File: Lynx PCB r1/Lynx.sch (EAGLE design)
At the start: 109 parts, among them IC1 LM321MF, IC3 ICL7660, Q1 8MHz

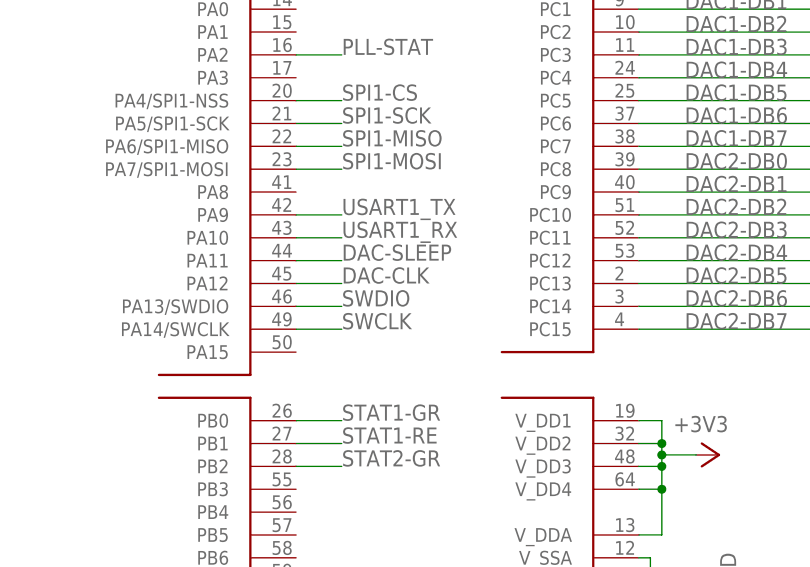
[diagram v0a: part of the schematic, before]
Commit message: Finished first pass of silk
Finished organizing the first revision of the artwork. Added pin names
to all busses. Created a dac-clk test pin
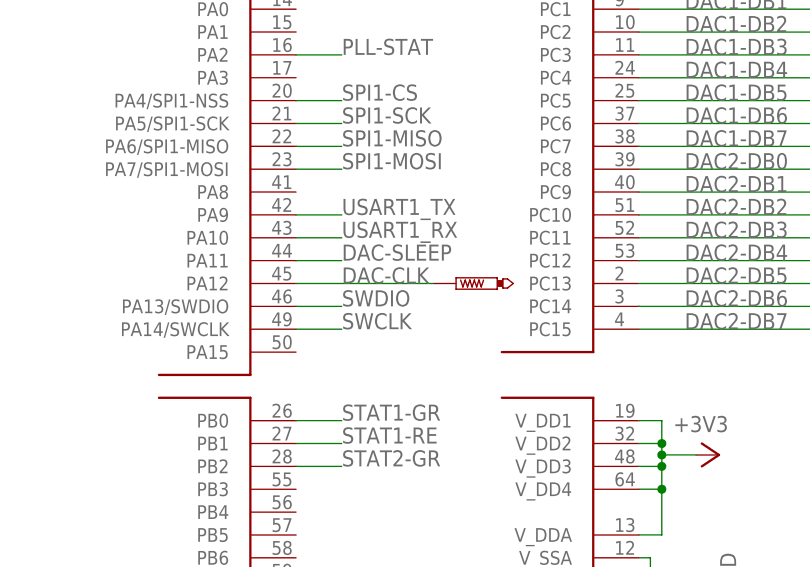
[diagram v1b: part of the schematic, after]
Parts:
- added DAC-CLK: PTR1PAD1-13Y, testpad:PTR1PAD1-13Y
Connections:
- net DAC-CLK: now also DAC-CLK.TP
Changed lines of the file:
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@@
 <grid distance="0.05" unitdist="inch" unit="inch" style="lines" multiple="1" display="no" altdistance="0.01" altunitdist="inch" altunit="inch"/>
 <layers>
-<layer number="1" name="Top" color="4" fill="1" visible="no" active="no"/>
-<layer number="2" name="Route2" color="1" fill="3" visible="no" active="no"/>
-<layer number="3" name="Route3" color="4" fill="3" visible="no" active="no"/>
-<layer number="4" name="Route4" color="1" fill="4" visible="no" active="no"/>
-<layer number="5" name="Route5" color="4" fill="4" visible="no" active="no"/>
-<layer number="6" name="Route6" color="1" fill="8" visible="no" active="no"/>
-<layer number="7" name="Route7" color="4" fill="8" visible="no" active="no"/>
-<layer number="8" name="Route8" color="1" fill="2" visible="no" active="no"/>
-<layer number="9" name="Route9" color="4" fill="2" visible="no" active="no"/>
-<layer number="10" name="Route10" color="1" fill="7" visible="no" active="no"/>
-<layer number="11" name="Route11" color="4" fill="7" visible="no" active="no"/>
-<layer number="12" name="Route12" color="1" fill="5" visible="no" active="no"/>
-<layer number="13" name="Route13" color="4" fill="5" visible="no" active="no"/>
-<layer number="14" name="Route14" color="1" fill="6" visible="no" active="no"/>
-<layer number="15" name="Route15" color="4" fill="6" visible="no" active="no"/>
-<layer number="16" name="Bottom" color="1" fill="1" visible="no" active="no"/>
-<layer number="17" name="Pads" color="2" fill="1" visible="no" active="no"/>
-<layer number="18" name="Vias" color="2" fill="1" visible="no" active="no"/>
-<layer number="19" name="Unrouted" color="6" fill="1" visible="no" active="no"/>
-<layer number="20" name="Dimension" color="15" fill="1" visible="no" active="no"/>
-<layer number="21" name="tPlace" color="7" fill="1" visible="no" active="no"/>
-<layer number="22" name="bPlace" color="7" fill="1" visible="no" active="no"/>
-<layer number="23" name="tOrigins" color="15" fill="1" visible="no" active="no"/>
-<layer number="24" name="bOrigins" color="15" fill="1" visible="no" active="no"/>
-<layer number="25" name="tNames" color="7" fill="1" visible="no" active="no"/>
-<layer number="26" name="bNames" color="7" fill="1" visible="no" active="no"/>
-<layer number="27" name="tValues" color="7" fill="1" visible="no" active="no"/>
-<layer number="28" name="bValues" color="7" fill="1" visible="no" active="no"/>
+<layer number="1" name="Top" color="4" fill="1" visible="yes" active="no"/>
+<layer number="2" name="Route2" color="1" fill="3" visible="yes" active="no"/>
+<layer number="3" name="Route3" color="4" fill="3" visible="yes" active="no"/>
+<layer number="4" name="Route4" color="1" fill="4" visible="yes" active="no"/>
+<layer number="5" name="Route5" color="4" fill="4" visible="yes" active="no"/>
+<layer number="6" name="Route6" color="1" fill="8" visible="yes" active="no"/>
+<layer number="7" name="Route7" color="4" fill="8" visible="yes" active="no"/>
+<layer number="8" name="Route8" color="1" fill="2" visible="yes" active="no"/>
+<layer number="9" name="Route9" color="4" fill="2" visible="yes" active="no"/>
+<layer number="10" name="Route10" color="1" fill="7" visible="yes" active="no"/>
+<layer number="11" name="Route11" color="4" fill="7" visible="yes" active="no"/>
+<layer number="12" name="Route12" color="1" fill="5" visible="yes" active="no"/>
+<layer number="13" name="Route13" color="4" fill="5" visible="yes" active="no"/>
+<layer number="14" name="Route14" color="1" fill="6" visible="yes" active="no"/>
+<layer number="15" name="Route15" color="4" fill="6" visible="yes" active="no"/>
+<layer number="16" name="Bottom" color="1" fill="1" visible="yes" active="no"/>
+<layer number="17" name="Pads" color="2" fill="1" visible="yes" active="no"/>
+<layer number="18" name="Vias" color="2" fill="1" visible="yes" active="no"/>
+<layer number="19" name="Unrouted" color="6" fill="1" visible="yes" active="no"/>
+<layer number="20" name="Dimension" color="15" fill="1" visible="yes" active="no"/>
+<layer number="21" name="tPlace" color="7" fill="1" visible="yes" active="no"/>
+<layer number="22" name="bPlace" color="7" fill="1" visible="yes" active="no"/>
+<layer number="23" name="tOrigins" color="15" fill="1" visible="yes" active="no"/>
+<layer number="24" name="bOrigins" color="15" fill="1" visible="yes" active="no"/>
+<layer number="25" name="tNames" color="7" fill="1" visible="yes" active="no"/>
+<layer number="26" name="bNames" color="7" fill="1" visible="yes" active="no"/>
+<layer number="27" name="tValues" color="7" fill="1" visible="yes" active="no"/>
+<layer number="28" name="bValues" color="7" fill="1" visible="yes" active="no"/>
 <layer number="29" name="tStop" color="7" fill="3" visible="no" active="no"/>
 <layer number="30" name="bStop" color="7" fill="6" visible="no" active="no"/>
@@
 <layer number="35" name="tGlue" color="7" fill="4" visible="no" active="no"/>
 <layer number="36" name="bGlue" color="7" fill="5" visible="no" active="no"/>
-<layer number="37" name="tTest" color="7" fill="1" visible="no" active="no"/>
-<layer number="38" name="bTest" color="7" fill="1" visible="no" active="no"/>
+<layer number="37" name="tTest" color="7" fill="1" visible="yes" active="no"/>
+<layer number="38" name="bTest" color="7" fill="1" visible="yes" active="no"/>
 <layer number="39" name="tKeepout" color="4" fill="11" visible="no" active="no"/>
 <layer number="40" name="bKeepout" color="1" fill="11" visible="no" active="no"/>
@@
 <layer number="44" name="Drills" color="7" fill="1" visible="no" active="no"/>
 <layer number="45" name="Holes" color="7" fill="1" visible="no" active="no"/>
-<layer number="46" name="Milling" color="3" fill="1" visible="no" active="no"/>
-<layer number="47" name="Measures" color="7" fill="1" visible="no" active="no"/>
-<layer number="48" name="Document" color="7" fill="1" visible="no" active="no"/>
-<layer number="49" name="Reference" color="7" fill="1" visible="no" active="no"/>
-<layer number="50" name="dxf" color="7" fill="1" visible="no" active="no"/>
-<layer number="51" name="tDocu" color="7" fill="1" visible="no" active="no"/>
-<layer number="52" name="bDocu" color="7" fill="1" visible="no" active="no"/>
-<layer number="53" name="tGND_GNDA" color="7" fill="9" visible="no" active="no"/>
-<layer number="54" name="bGND_GNDA" color="1" fill="9" visible="no" active="no"/>
-<layer number="56" name="wert" color="7" fill="1" visible="no" active="no"/>
+<layer number="46" name="Milling" color="3" fill="1" visible="yes" active="no"/>
+<layer number="47" name="Measures" color="7" fill="1" visible="yes" active="no"/>
+<layer number="48" name="Document" color="7" fill="1" visible="yes" active="no"/>
+<layer number="49" name="Reference" color="7" fill="1" visible="yes" active="no"/>
+<layer number="50" name="dxf" color="7" fill="1" visible="yes" active="no"/>
+<layer number="51" name="tDocu" color="7" fill="1" visible="yes" active="no"/>
+<layer number="52" name="bDocu" color="7" fill="1" visible="yes" active="no"/>
+<layer number="53" name="tGND_GNDA" color="7" fill="9" visible="yes" active="no"/>
+<layer number="54" name="bGND_GNDA" color="1" fill="9" visible="yes" active="no"/>
+<layer number="56" name="wert" color="7" fill="1" visible="yes" active="no"/>
 <layer number="91" name="Nets" color="2" fill="1" visible="yes" active="yes"/>
 <layer number="92" name="Busses" color="1" fill="1" visible="yes" active="yes"/>
@@
 <part name="SUPPLY59" library="supply2" deviceset="GND" device=""/>
 <part name="JP11" library="pinhead" deviceset="PINHD-1X2" device="" value="Power In"/>
+<part name="DAC-CLK" library="testpad" deviceset="PTR1" device="PAD1-13Y" value="PTR1PAD1-13Y"/>
 </parts>
 <sheets>
@@
 <instance part="SUPPLY59" gate="GND" x="85.09" y="-44.45" rot="MR0"/>
 <instance part="JP11" gate="G$1" x="-243.84" y="-168.91" rot="R180"/>
+<instance part="DAC-CLK" gate="G$1" x="-198.12" y="29.21" smashed="yes" rot="R90">
+<attribute name="TP_SIGNAL_NAME" x="-195.58" y="30.48" size="1.778" layer="97" rot="R90"/>
+</instance>
 </instances>
 <busses>
@@
 <segment>
 <pinref part="U$1" gate="PORT_A" pin="PA12"/>
-<wire x1="-215.9" y1="29.21" x2="-210.82" y2="29.21" width="0.1524" layer="91"/>
 <label x="-210.82" y="29.21" size="1.778" layer="95"/>
-</segment>
-</net>
+<pinref part="DAC-CLK" gate="G$1" pin="TP"/>
+<wire x1="-200.66" y1="29.21" x2="-215.9" y2="29.21" width="0.1524" layer="91"/>
+</segment>
+</net>

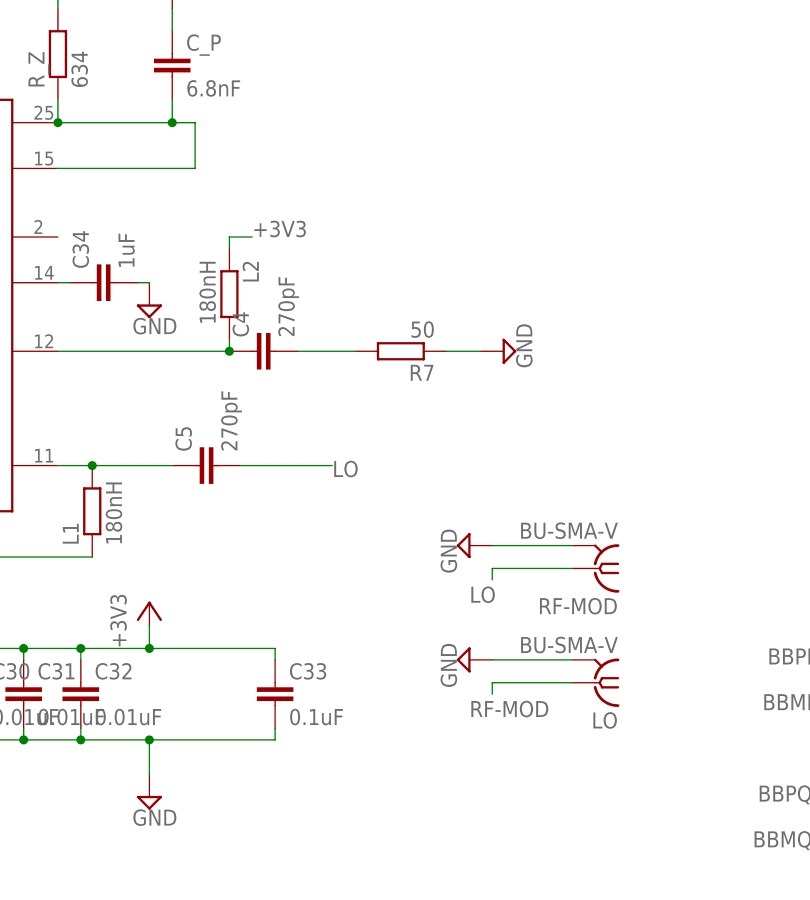
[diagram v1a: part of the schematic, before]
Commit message: Changes as per Cillian
Changed the layout of the RF
swapped out the coax connectors
added "TUNE" test point
revamped the ground planes
stitched the ground planes (a lot)
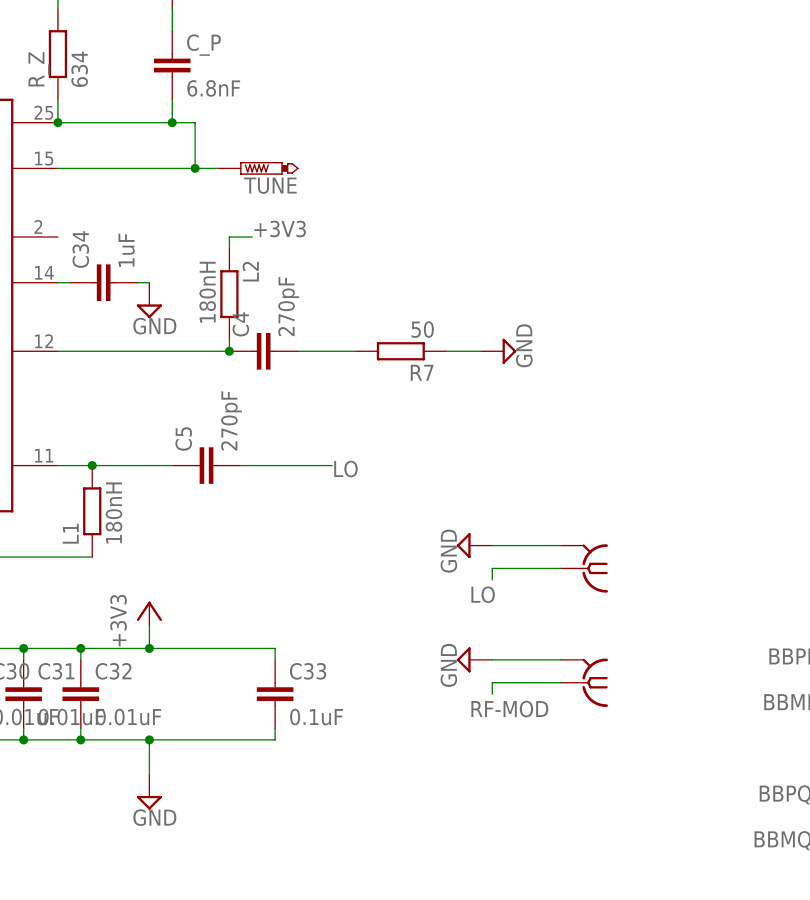
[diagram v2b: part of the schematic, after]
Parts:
- added TUNE: PTR1B1,27, testpad:PTR1B1,27
- C31, C6, C7: device rcl:C-EUC0603 -> rcl:C-EUC0402
- LO, RF-MOD: value BU-SMA-V -> SMA-142-0711-821/826; device con-coax:BU-SMA-V -> con-coax:SMA-142-0711-821/826
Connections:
- net N$9 renamed RF+
- net LO: now also LO.1; no longer RF-MOD.1
- net N$1: now also TUNE.TP
- net RF-MOD: now also RF-MOD.1; no longer LO.1
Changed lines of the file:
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@@
 <part name="SUPPLY15" library="supply2" deviceset="GND" device=""/>
 <part name="+3V5" library="supply1" deviceset="+3V3" device=""/>
-<part name="C6" library="rcl" deviceset="C-EU" device="C0603" value="470pf"/>
-<part name="C7" library="rcl" deviceset="C-EU" device="C0603" value="470pf"/>
+<part name="C6" library="rcl" deviceset="C-EU" device="C0402" value="470pf"/>
+<part name="C7" library="rcl" deviceset="C-EU" device="C0402" value="470pf"/>
 <part name="SUPPLY16" library="supply2" deviceset="GND" device=""/>
 <part name="10MHZ" library="Lynx components" deviceset="TCXO" device=""/>
@@
 <part name="SUPPLY34" library="supply2" deviceset="GND" device=""/>
 <part name="+3V12" library="supply1" deviceset="+3V3" device=""/>
-<part name="RF-MOD" library="con-coax" deviceset="BU-SMA-V" device=""/>
 <part name="SUPPLY35" library="supply2" deviceset="GND" device=""/>
 <part name="R8" library="rcl" deviceset="R-EU_" device="R0603" value="15"/>
@@
 <attribute name="ARM" value=""/>
 </part>
-<part name="C31" library="rcl" deviceset="C-EU" device="C0603" value="0.01uF">
+<part name="C31" library="rcl" deviceset="C-EU" device="C0402" value="0.01uF">
 <attribute name="ARM" value=""/>
 </part>
@@
 <part name="SUPPLY57" library="supply2" deviceset="GND" device=""/>
 <part name="BOOT0" library="switch-tact" deviceset="DTSM-6" device=""/>
-<part name="LO" library="con-coax" deviceset="BU-SMA-V" device=""/>
 <part name="SUPPLY54" library="supply2" deviceset="GND" device=""/>
 <part name="+3V1" library="supply1" deviceset="+3V3" device=""/>
@@
 <part name="JP11" library="pinhead" deviceset="PINHD-1X2" device="" value="Power In"/>
 <part name="DAC-CLK" library="testpad" deviceset="PTR1" device="PAD1-13Y" value="PTR1PAD1-13Y"/>
+<part name="TUNE" library="testpad" deviceset="PTR1" device="B1,27" value="PTR1B1,27"/>
+<part name="LO" library="con-coax" deviceset="SMA-" device="142-0711-821/826"/>
+<part name="RF-MOD" library="con-coax" deviceset="SMA-" device="142-0711-821/826"/>
 </parts>
 <sheets>
@@
 <instance part="SUPPLY34" gate="GND" x="-29.21" y="-77.47" rot="R180"/>
 <instance part="+3V12" gate="G$1" x="-29.21" y="-95.25" rot="R180"/>
-<instance part="RF-MOD" gate="G$1" x="140.97" y="102.87" rot="R180"/>
 <instance part="SUPPLY35" gate="GND" x="127" y="105.41" rot="R270"/>
 <instance part="SUPPLY38" gate="GND" x="-212.09" y="-124.46"/>
@@
 <instance part="SUPPLY57" gate="GND" x="-170.18" y="69.85"/>
 <instance part="BOOT0" gate="G$1" x="-157.48" y="83.82" rot="R90"/>
-<instance part="LO" gate="G$1" x="140.97" y="90.17" rot="R180"/>
 <instance part="SUPPLY54" gate="GND" x="127" y="92.71" rot="R270"/>
 <instance part="U$3" gate="G$1" x="63.5" y="142.24"/>
@@
 <attribute name="TP_SIGNAL_NAME" x="-195.58" y="30.48" size="1.778" layer="97" rot="R90"/>
 </instance>
+<instance part="TUNE" gate="G$1" x="101.6" y="147.32" rot="R90"/>
+<instance part="LO" gate="G1" x="139.7" y="102.87" smashed="yes" rot="R180"/>
+<instance part="RF-MOD" gate="G1" x="139.7" y="90.17" smashed="yes" rot="R180"/>
 </instances>
 <busses>
@@
 </segment>
 <segment>
-<pinref part="RF-MOD" gate="G$1" pin="2"/>
-<wire x1="138.43" y1="105.41" x2="129.54" y2="105.41" width="0.1524" layer="91"/>
-<pinref part="SUPPLY35" gate="GND" pin="GND"/>
-</segment>
-<segment>
 <pinref part="SUPPLY38" gate="GND" pin="GND"/>
 <wire x1="-212.09" y1="-116.84" x2="-212.09" y2="-121.92" width="0.1524" layer="91"/>
@@
 <pinref part="R13" gate="G$1" pin="1"/>
 <wire x1="-170.18" y1="72.39" x2="-170.18" y2="76.2" width="0.1524" layer="91"/>
-</segment>
-<segment>
-<pinref part="LO" gate="G$1" pin="2"/>
-<wire x1="138.43" y1="92.71" x2="129.54" y2="92.71" width="0.1524" layer="91"/>
-<pinref part="SUPPLY54" gate="GND" pin="GND"/>
 </segment>
 <segment>
@@
 <label x="-231.14" y="-171.45" size="1.778" layer="95"/>
 </segment>
+<segment>
+<pinref part="SUPPLY35" gate="GND" pin="GND"/>
+<pinref part="LO" gate="G1" pin="2"/>
+<wire x1="129.54" y1="105.41" x2="137.16" y2="105.41" width="0.1524" layer="91"/>
+</segment>
+<segment>
+<pinref part="SUPPLY54" gate="GND" pin="GND"/>
+<pinref part="RF-MOD" gate="G1" pin="2"/>
+<wire x1="129.54" y1="92.71" x2="137.16" y2="92.71" width="0.1524" layer="91"/>
+</segment>
 </net>
 <net name="BBPI" class="0">
@@
 </segment>
 <segment>
-<pinref part="RF-MOD" gate="G$1" pin="1"/>
-<wire x1="138.43" y1="102.87" x2="129.54" y2="102.87" width="0.1524" layer="91"/>
 <wire x1="129.54" y1="102.87" x2="129.54" y2="101.6" width="0.1524" layer="91"/>
 <label x="127" y="99.06" size="1.778" layer="95"/>
+<pinref part="LO" gate="G1" pin="1"/>
+<wire x1="129.54" y1="102.87" x2="137.16" y2="102.87" width="0.1524" layer="91"/>
 </segment>
 <segment>
@@
 </segment>
 <segment>
-<pinref part="LO" gate="G$1" pin="1"/>
-<wire x1="138.43" y1="90.17" x2="129.54" y2="90.17" width="0.1524" layer="91"/>
 <wire x1="129.54" y1="90.17" x2="129.54" y2="88.9" width="0.1524" layer="91"/>
 <label x="127" y="86.36" size="1.778" layer="95"/>
+<pinref part="RF-MOD" gate="G1" pin="1"/>
+<wire x1="129.54" y1="90.17" x2="137.16" y2="90.17" width="0.1524" layer="91"/>
 </segment>
 </net>
@@
 <junction x="81.28" y="152.4"/>
 <junction x="93.98" y="152.4"/>
+<pinref part="TUNE" gate="G$1" pin="TP"/>
+<wire x1="99.06" y1="147.32" x2="96.52" y2="147.32" width="0.1524" layer="91"/>
+<junction x="96.52" y="147.32"/>
 </segment>
 </net>
@@
 </segment>
 </net>
-<net name="N$9" class="0">
+<net name="RF+" class="0">
 <segment>
 <pinref part="U$3" gate="G$1" pin="RF+"/>
